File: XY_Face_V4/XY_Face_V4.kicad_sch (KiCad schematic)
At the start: 37 parts, among them CN1 DF11-2DSA-4DP, J11 DF11-4DP-2DSA, J13 DF11-4DP-2DSA, J2 Conn_01x01, J3 Conn_01x01, J4 Conn_01x01, J5 Conn_01x01, Q2 CSD17576Q5B, U1 VEML7700, U2 TMP112xxDRL, U3 DRV2605LDGS, U4 TCA4311ADGKR, U5 5040500691, U6 5040500691

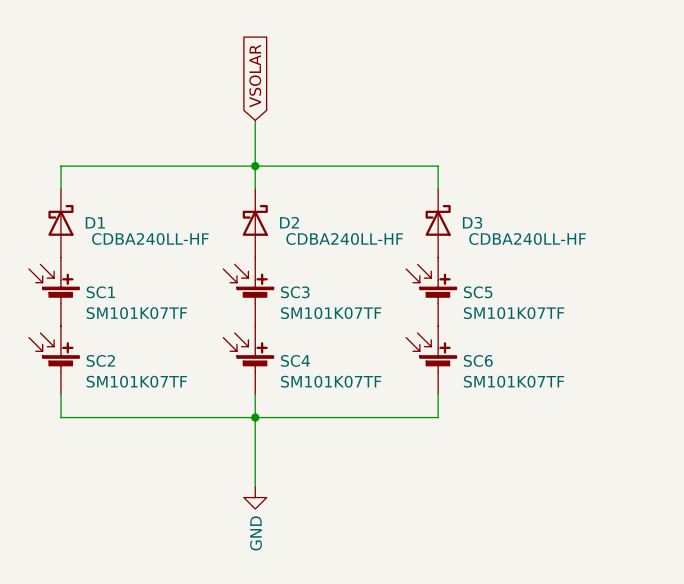
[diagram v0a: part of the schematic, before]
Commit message: Removed 2p Solar Cells
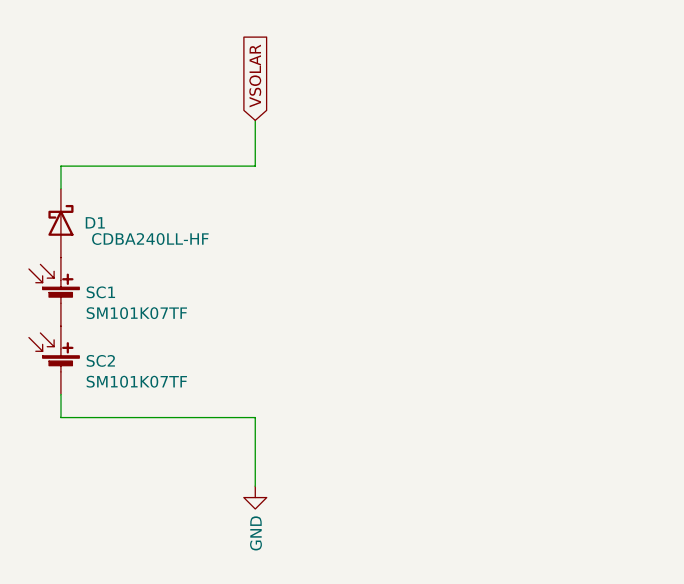
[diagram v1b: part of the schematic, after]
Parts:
- removed D2, D3: CDBA240LL-HF, SolarPanelBoards:DO-214AC, symbol Device:D_Schottky
- removed SC3, SC4, SC5, SC6: SM101K07TF, SolarPanelBoards:KXOB101K08F-TR, symbol Device:Solar_Cell

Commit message: V4: Added new Cells to Footprint
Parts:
- removed U1: VEML7700, VEML7700-TT:XDCR_VEML7700-TT, symbol Adafruit VEML7700-eagle-import:VEML7700
- added U7: VEML6031X00, easyeda2kicad:SENSOR-SMD_VEML6031X00, symbol easyeda2kicad:VEML6031X00
- SC1, SC2: value SM101K07TF -> SM261K10TF; footprint SolarPanelBoards:KXOB101K08F-TR -> Solar_Cell_Library:SM261K10TF
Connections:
- net +3V3: now also U7.6 (VDD)
- net GND: now also U7.1 (GND), U7.4 (GND)
- net SCL: now also U7.5 (SCL)
- net SDA: now also U7.2 (SDA)
- no-connect marks 9 -> 10
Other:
- moved on the sheet: D1, SC1, SC2
